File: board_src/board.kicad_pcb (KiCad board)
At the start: 2 copper layers, 220 x 150 mm, 149 parts, among them IC1 PCF8563TS_4,118, IC2 M24C02-WMN6TP, IC3 DS18B20+, IC4 FT232RNL-TUBE, IC5 MCP3202, IC6 MCP4921-E_P, J1 Conn_01x05, J10 Conn_01x02_Pin, J11 Conn_01x03, J12 112J-TDAR-R01, J13 Conn_01x03, J14 Conn_01x07, J15 Conn_01x03, J16 Conn_01x05, J17 Conn_01x05, J18 Conn_02x20_Counter_Clockwise, J19 Conn_02x07_Odd_Even, J2 Conn_01x05, J20 Conn_02x20_Counter_Clockwise, J21 Conn_02x20_Counter_Clockwise, J22 Conn_02x20_Counter_Clockwise, J23 Conn_01x04, J24 Conn_01x08, J25 Conn_01x04, J26 Conn_01x20_Socket, J27 Conn_01x20_Socket, J28 Conn_01x04, J29 Conn_01x08, J3 Conn_01x06, J30 Conn_01x05, J31 Conn_01x05, J32 Conn_02x05_Odd_Even, J33 Conn_01x02_Pin, J34 USB_C_Receptacle_USB2.0_16P, J36 Conn_01x20_Socket, J37 Conn_01x20_Socket, J4 Conn_01x04, J40 Conn_01x01_Pin, J41 Conn_01x01_Pin, J42 Conn_01x01_Pin, J43 Conn_01x01_Pin, J44 Conn_01x01_Pin, J46 Conn_01x01_Pin, J5 Conn_01x08, J6 Conn_01x02_Pin, J7 Conn_01x16_Socket, J8 Conn_01x04, J9 Conn_01x02_Pin, Q1 NPN, Q2 SS8550, Q3 SS8550, Q4 SS8550, Q5 SS8550, Q6 BSS123, Q7 BC107, Y2 Crystal

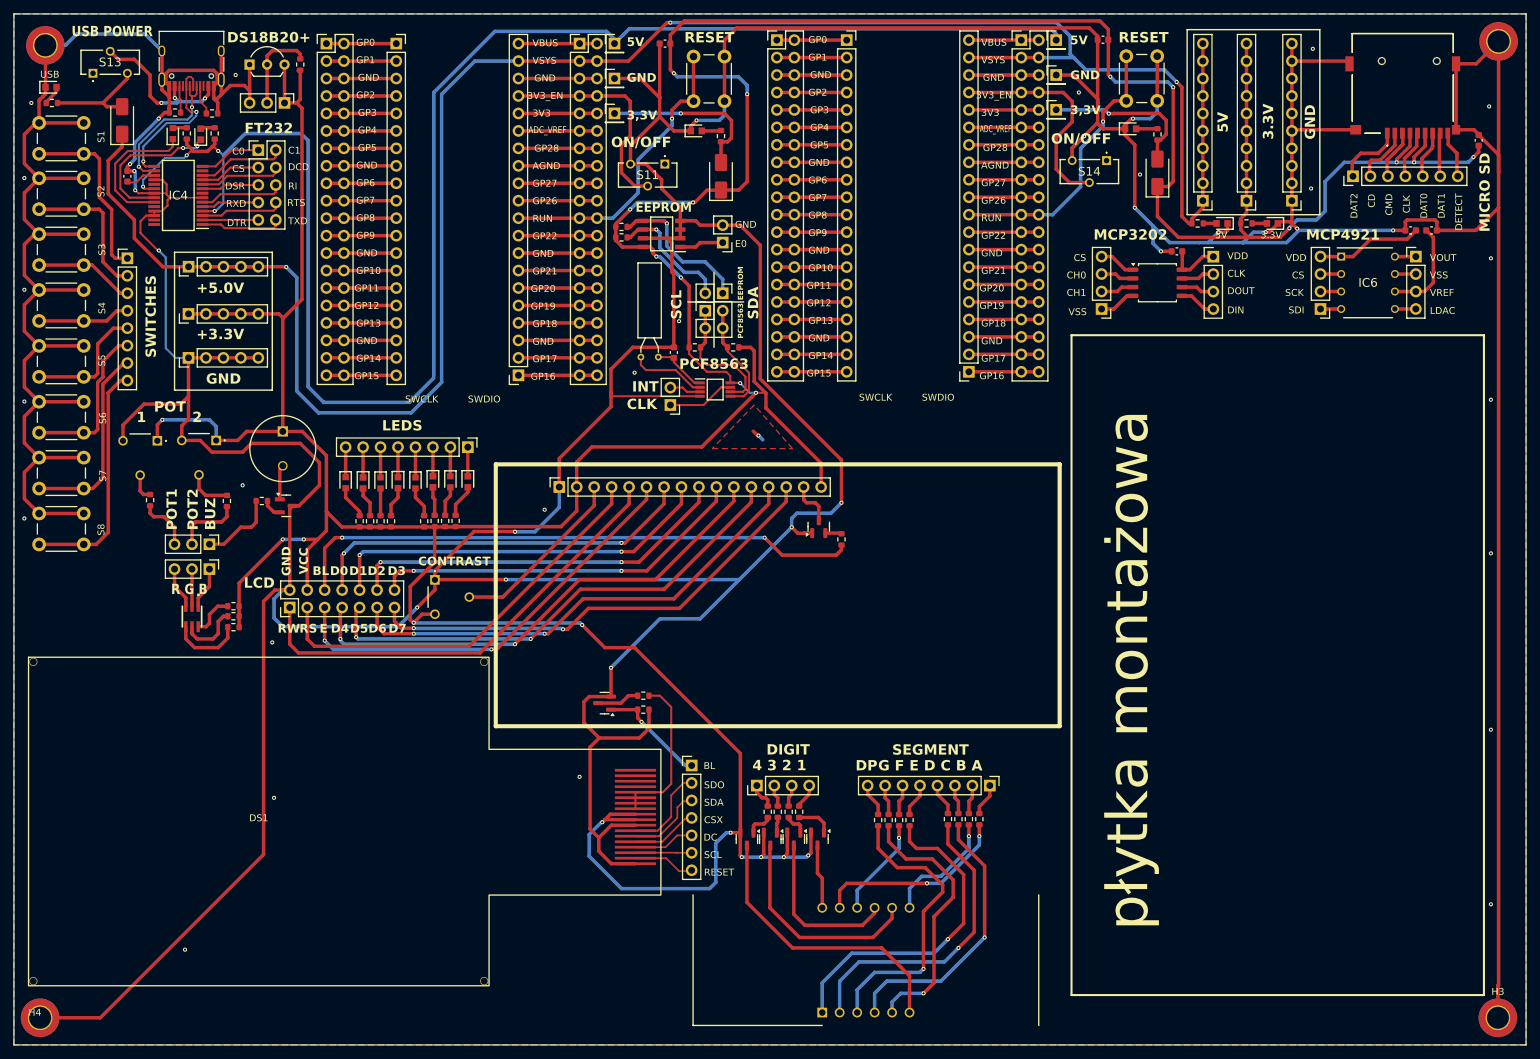
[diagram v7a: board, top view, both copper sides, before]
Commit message: Poprawki w schematach. Rozpoczęte korekty płytki
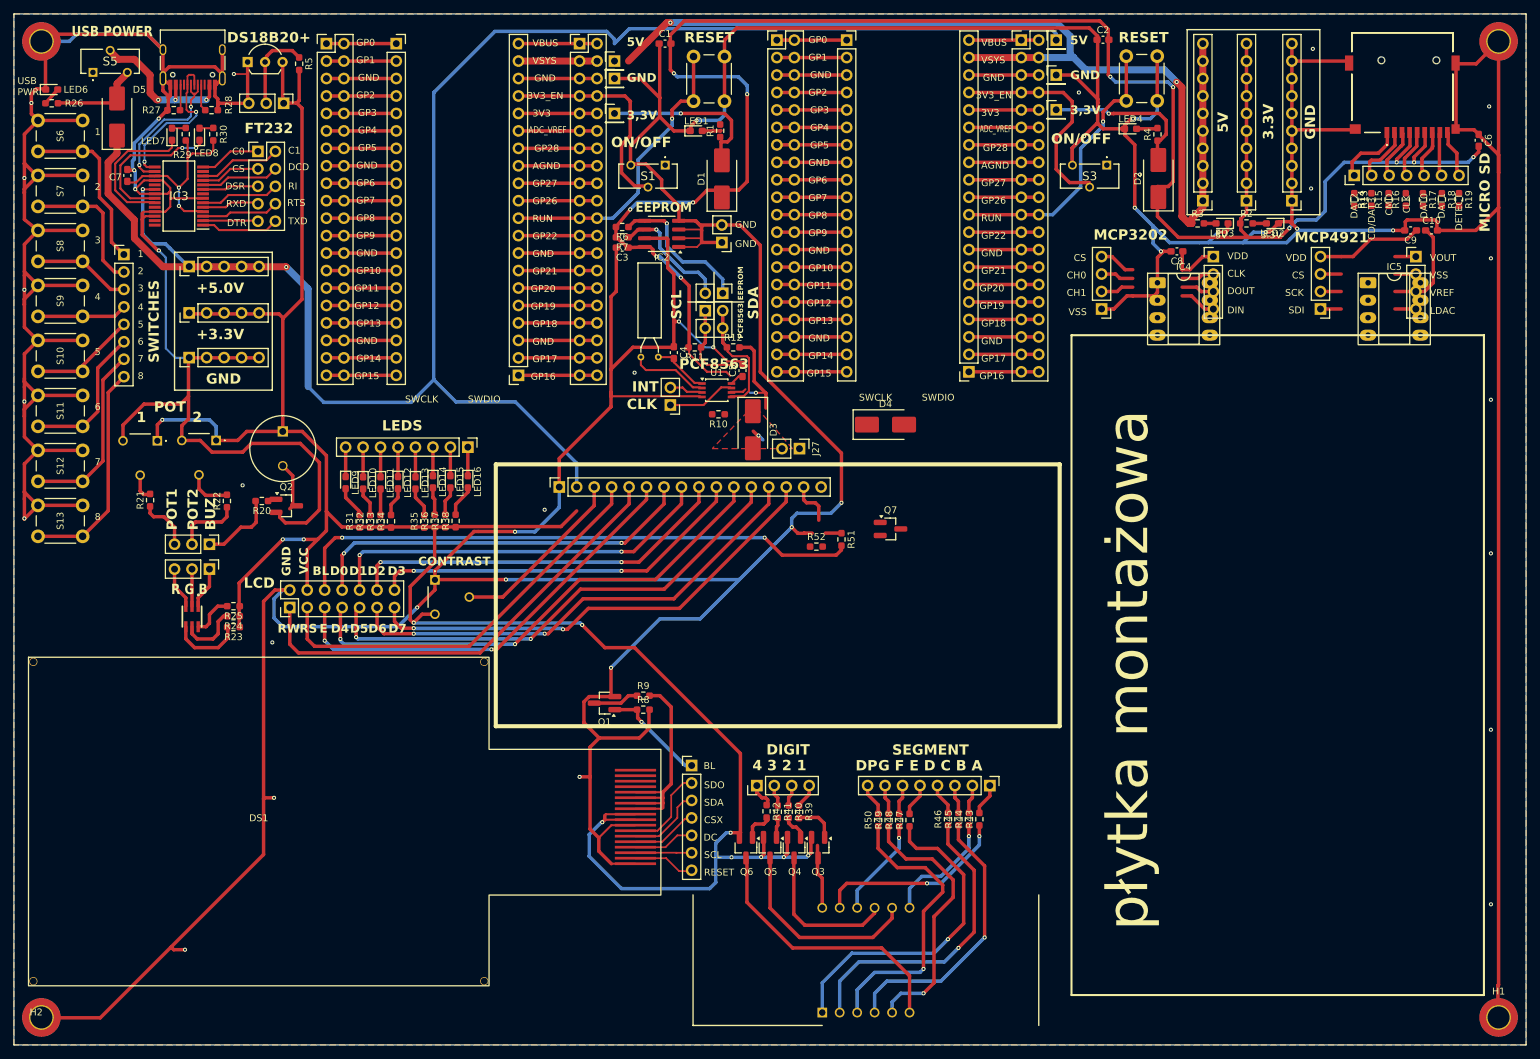
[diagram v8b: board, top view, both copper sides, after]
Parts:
- removed the IC1 at (102.0, 54.7)
- added C3: 100n, Capacitor_SMD:C_0603_1608Metric_Pad1.08x0.95mm_HandSolder, F.Cu at (88.5, 34.0)
- added C5: 100n, Capacitor_SMD:C_0603_1608Metric_Pad1.08x0.95mm_HandSolder, F.Cu at (106.0, 51.9)
- added D1: VS-10BQ015-M3/5BT, Diode_SMD:D_SMB_Handsoldering, F.Cu at (103.0, 24.0)
- added D3: VS-10BQ015-M3/5BT, Diode_SMD:D_SMB_Handsoldering, F.Cu at (107.5, 60.5)
- added J27: Battery, Connector_PinHeader_2.54mm:PinHeader_1x02_P2.54mm_Vertical, F.Cu at (114.3, 63.2)
- added R10: 47k, Resistor_SMD:R_0603_1608Metric_Pad0.98x0.95mm_HandSolder, F.Cu at (102.5, 58.2)
- added R13: 47k, Resistor_SMD:R_0603_1608Metric_Pad0.98x0.95mm_HandSolder, F.Cu at (195.0, 27.0)
- added R14: 47k, Resistor_SMD:R_0603_1608Metric_Pad0.98x0.95mm_HandSolder, F.Cu at (197.5, 27.0)
- added R15: 47k, Resistor_SMD:R_0603_1608Metric_Pad0.98x0.95mm_HandSolder, F.Cu at (200.0, 27.0)
- added R16: 47k, Resistor_SMD:R_0603_1608Metric_Pad0.98x0.95mm_HandSolder, F.Cu at (202.5, 27.0)
- added R17: 47k, Resistor_SMD:R_0603_1608Metric_Pad0.98x0.95mm_HandSolder, F.Cu at (205.0, 27.0)
- added R18: 47k, Resistor_SMD:R_0603_1608Metric_Pad0.98x0.95mm_HandSolder, F.Cu at (207.8, 27.0)
- added R19: 47k, Resistor_SMD:R_0603_1608Metric_Pad0.98x0.95mm_HandSolder, F.Cu at (210.2, 27.0)
- added R52: 50, Resistor_SMD:R_0603_1608Metric_Pad0.98x0.95mm_HandSolder, F.Cu at (116.8, 77.5)
- added U1: PCF8563TS, Package_SO:TSSOP-8_3x3mm_P0.65mm, F.Cu at (102.2, 54.8)
- C1: renamed from C5; footprint Capacitor_SMD:C_0603_1608Metric -> Capacitor_SMD:C_0603_1608Metric_Pad1.08x0.95mm_HandSolder
- C10: renamed from C8; footprint Capacitor_SMD:C_0603_1608Metric -> Capacitor_SMD:C_0603_1608Metric_Pad1.08x0.95mm_HandSolder
- C2: renamed from C6; footprint Capacitor_SMD:C_0603_1608Metric -> Capacitor_SMD:C_0603_1608Metric_Pad1.08x0.95mm_HandSolder
- C4: renamed from C1; value 100n -> 10p; footprint Capacitor_SMD:C_0603_1608Metric -> Capacitor_SMD:C_0603_1608Metric_Pad1.08x0.95mm_HandSolder
- C6: renamed from C3; footprint Capacitor_SMD:C_0603_1608Metric -> Capacitor_SMD:C_0603_1608Metric_Pad1.08x0.95mm_HandSolder
- C7: renamed from C2; value C_Small -> 100n; footprint Capacitor_SMD:C_0603_1608Metric -> Capacitor_SMD:C_0603_1608Metric_Pad1.08x0.95mm_HandSolder
- C8: renamed from C4; footprint Capacitor_SMD:C_0603_1608Metric -> Capacitor_SMD:C_0603_1608Metric_Pad1.08x0.95mm_HandSolder
- C9: renamed from C7; footprint Capacitor_SMD:C_0603_1608Metric -> Capacitor_SMD:C_0603_1608Metric_Pad1.08x0.95mm_HandSolder
- D2, D4, D5: value D_Schottky -> VS-10BQ015-M3/5BT; footprint Diode_SMD:D_SMA -> Diode_SMD:D_SMB_Handsoldering
- IC2: footprint footprints:EEPROM -> Package_SO:SOIC-8_3.9x4.9mm_P1.27mm
- IC4: renamed from IC5; footprint Package_SO:SOIC-8_5.3x5.3mm_P1.27mm -> Package_DIP:DIP-8_W7.62mm_Socket_LongPads
- IC5: renamed from IC6; footprint footprints:DIP781W56P254L950H533Q8N -> Package_DIP:DIP-8_W7.62mm_Socket_LongPads
- LED1: renamed from LED14; footprint footprints:LEDC1608X100N -> LED_SMD:LED_0603_1608Metric_Pad1.05x0.95mm_HandSolder
- LED10: renamed from LED6; footprint footprints:LEDC1608X100N -> LED_SMD:LED_0603_1608Metric_Pad1.05x0.95mm_HandSolder
- LED11: renamed from LED3; footprint footprints:LEDC1608X80N -> LED_SMD:LED_0603_1608Metric_Pad1.05x0.95mm_HandSolder
- LED12: renamed from LED7; footprint footprints:LEDC1608X100N -> LED_SMD:LED_0603_1608Metric_Pad1.05x0.95mm_HandSolder
- LED13: renamed from LED4; footprint footprints:LEDC1608X80N -> LED_SMD:LED_0603_1608Metric_Pad1.05x0.95mm_HandSolder
- LED14: renamed from LED8; footprint footprints:LEDC1608X100N -> LED_SMD:LED_0603_1608Metric_Pad1.05x0.95mm_HandSolder
- LED15: renamed from LED5; footprint footprints:LEDC1608X80N -> LED_SMD:LED_0603_1608Metric_Pad1.05x0.95mm_HandSolder
- LED16: renamed from LED9; footprint footprints:LEDC1608X100N -> LED_SMD:LED_0603_1608Metric_Pad1.05x0.95mm_HandSolder
- LED2: renamed from LED16; footprint footprints:LEDC1608X100N -> LED_SMD:LED_0603_1608Metric_Pad1.05x0.95mm_HandSolder
- LED3: renamed from LED17; footprint footprints:LEDC1608X100N -> LED_SMD:LED_0603_1608Metric_Pad1.05x0.95mm_HandSolder
- LED4: renamed from LED15; footprint footprints:LEDC1608X100N -> LED_SMD:LED_0603_1608Metric_Pad1.05x0.95mm_HandSolder
- LED6: renamed from LED18; footprint footprints:LEDC1608X100N -> LED_SMD:LED_0603_1608Metric_Pad1.05x0.95mm_HandSolder
- LED7: renamed from LED10; footprint footprints:LEDC1608X80N -> LED_SMD:LED_0603_1608Metric_Pad1.05x0.95mm_HandSolder
- LED8: renamed from LED11; footprint footprints:LEDC1608X100N -> LED_SMD:LED_0603_1608Metric_Pad1.05x0.95mm_HandSolder
- LED9: renamed from LED2; footprint footprints:LEDC1608X80N -> LED_SMD:LED_0603_1608Metric_Pad1.05x0.95mm_HandSolder
- LS1: value BMT0905XH05 -> UGCM0903XP4.5IC
- Q1: renamed from Q6; footprint Package_TO_SOT_SMD:SOT-23 -> Package_TO_SOT_SMD:SOT-23_Handsoldering
- Q2: renamed from Q1; value NPN -> SS8050-L; footprint Package_TO_SOT_SMD:SOT-23 -> Package_TO_SOT_SMD:SOT-23_Handsoldering
- Q3: renamed from Q2; value SS8550 -> SS8550-L; footprint Package_TO_SOT_SMD:SOT-23 -> Package_TO_SOT_SMD:SOT-23_Handsoldering
- Q4: renamed from Q3; value SS8550 -> SS8550-L; footprint Package_TO_SOT_SMD:SOT-23 -> Package_TO_SOT_SMD:SOT-23_Handsoldering
- Q5: renamed from Q4; value SS8550 -> SS8550-L; footprint Package_TO_SOT_SMD:SOT-23 -> Package_TO_SOT_SMD:SOT-23_Handsoldering
- Q6: renamed from Q5; value SS8550 -> SS8550-L; footprint Package_TO_SOT_SMD:SOT-23 -> Package_TO_SOT_SMD:SOT-23_Handsoldering
- Q7: value BC107 -> SS8050-L; footprint Package_TO_SOT_SMD:SOT-23 -> Package_TO_SOT_SMD:SOT-23_Handsoldering
- R1: renamed from R6; footprint Resistor_SMD:R_0603_1608Metric -> Resistor_SMD:R_0603_1608Metric_Pad0.98x0.95mm_HandSolder
- R11: renamed from R43; value 4.7k -> 10k; footprint Resistor_SMD:R_0603_1608Metric -> Resistor_SMD:R_0603_1608Metric_Pad0.98x0.95mm_HandSolder
- R12: renamed from R44; value 4.7k -> 10k; footprint Resistor_SMD:R_0603_1608Metric -> Resistor_SMD:R_0603_1608Metric_Pad0.98x0.95mm_HandSolder
- R2: renamed from R8; footprint Resistor_SMD:R_0603_1608Metric -> Resistor_SMD:R_0603_1608Metric_Pad0.98x0.95mm_HandSolder
- R20: value 450 -> 4.7k; footprint Resistor_SMD:R_0603_1608Metric -> Resistor_SMD:R_0603_1608Metric_Pad0.98x0.95mm_HandSolder
- R21: renamed from R2; value 270 -> 27; footprint Resistor_SMD:R_0603_1608Metric -> Resistor_SMD:R_0603_1608Metric_Pad0.98x0.95mm_HandSolder
- R22: renamed from R14; value 270 -> 27; footprint Resistor_SMD:R_0603_1608Metric -> Resistor_SMD:R_0603_1608Metric_Pad0.98x0.95mm_HandSolder
- R23: footprint Resistor_SMD:R_0603_1608Metric -> Resistor_SMD:R_0603_1608Metric_Pad0.98x0.95mm_HandSolder
- R24: renamed from R22; footprint Resistor_SMD:R_0603_1608Metric -> Resistor_SMD:R_0603_1608Metric_Pad0.98x0.95mm_HandSolder
- R25: renamed from R21; footprint Resistor_SMD:R_0603_1608Metric -> Resistor_SMD:R_0603_1608Metric_Pad0.98x0.95mm_HandSolder
- R26: renamed from R10; value 249 -> 330; footprint Resistor_SMD:R_0603_1608Metric -> Resistor_SMD:R_0603_1608Metric_Pad0.98x0.95mm_HandSolder
- R27: renamed from R46; footprint Resistor_SMD:R_0603_1608Metric -> Resistor_SMD:R_0603_1608Metric_Pad0.98x0.95mm_HandSolder
- R28: renamed from R45; footprint Resistor_SMD:R_0603_1608Metric -> Resistor_SMD:R_0603_1608Metric_Pad0.98x0.95mm_HandSolder
- R29: renamed from R5; value 1k -> 220; footprint Resistor_SMD:R_0603_1608Metric -> Resistor_SMD:R_0603_1608Metric_Pad0.98x0.95mm_HandSolder
- R3: renamed from R9; footprint Resistor_SMD:R_0603_1608Metric -> Resistor_SMD:R_0603_1608Metric_Pad0.98x0.95mm_HandSolder
- R30: renamed from R3; value 1k -> 220; footprint Resistor_SMD:R_0603_1608Metric -> Resistor_SMD:R_0603_1608Metric_Pad0.98x0.95mm_HandSolder
- R31: renamed from R11; footprint Resistor_SMD:R_0603_1608Metric -> Resistor_SMD:R_0603_1608Metric_Pad0.98x0.95mm_HandSolder
- R32: renamed from R12; footprint Resistor_SMD:R_0603_1608Metric -> Resistor_SMD:R_0603_1608Metric_Pad0.98x0.95mm_HandSolder
- R33: renamed from R37; footprint Resistor_SMD:R_0603_1608Metric -> Resistor_SMD:R_0603_1608Metric_Pad0.98x0.95mm_HandSolder
- R34: renamed from R38; footprint Resistor_SMD:R_0603_1608Metric -> Resistor_SMD:R_0603_1608Metric_Pad0.98x0.95mm_HandSolder
- R35: renamed from R39; footprint Resistor_SMD:R_0603_1608Metric -> Resistor_SMD:R_0603_1608Metric_Pad0.98x0.95mm_HandSolder
- R36: renamed from R40; footprint Resistor_SMD:R_0603_1608Metric -> Resistor_SMD:R_0603_1608Metric_Pad0.98x0.95mm_HandSolder
- R37: renamed from R41; footprint Resistor_SMD:R_0603_1608Metric -> Resistor_SMD:R_0603_1608Metric_Pad0.98x0.95mm_HandSolder
- R38: renamed from R42; footprint Resistor_SMD:R_0603_1608Metric -> Resistor_SMD:R_0603_1608Metric_Pad0.98x0.95mm_HandSolder
- R39: renamed from R31; footprint Resistor_SMD:R_0603_1608Metric -> Resistor_SMD:R_0603_1608Metric_Pad0.98x0.95mm_HandSolder
- R4: renamed from R7; footprint Resistor_SMD:R_0603_1608Metric -> Resistor_SMD:R_0603_1608Metric_Pad0.98x0.95mm_HandSolder
- R40: renamed from R32; footprint Resistor_SMD:R_0603_1608Metric -> Resistor_SMD:R_0603_1608Metric_Pad0.98x0.95mm_HandSolder
- R41: renamed from R33; footprint Resistor_SMD:R_0603_1608Metric -> Resistor_SMD:R_0603_1608Metric_Pad0.98x0.95mm_HandSolder
- R42: renamed from R34; footprint Resistor_SMD:R_0603_1608Metric -> Resistor_SMD:R_0603_1608Metric_Pad0.98x0.95mm_HandSolder
- R43: renamed from R13; value 220 -> 330; footprint Resistor_SMD:R_0603_1608Metric -> Resistor_SMD:R_0603_1608Metric_Pad0.98x0.95mm_HandSolder
- R44: renamed from R24; footprint Resistor_SMD:R_0603_1608Metric -> Resistor_SMD:R_0603_1608Metric_Pad0.98x0.95mm_HandSolder
- R45: renamed from R25; value 220 -> 330; footprint Resistor_SMD:R_0603_1608Metric -> Resistor_SMD:R_0603_1608Metric_Pad0.98x0.95mm_HandSolder
- R46: renamed from R26; value 220 -> 330; footprint Resistor_SMD:R_0603_1608Metric -> Resistor_SMD:R_0603_1608Metric_Pad0.98x0.95mm_HandSolder
- R47: renamed from R27; value 220 -> 330; footprint Resistor_SMD:R_0603_1608Metric -> Resistor_SMD:R_0603_1608Metric_Pad0.98x0.95mm_HandSolder
- R48: renamed from R28; value 220 -> 330; footprint Resistor_SMD:R_0603_1608Metric -> Resistor_SMD:R_0603_1608Metric_Pad0.98x0.95mm_HandSolder
- R49: renamed from R29; value 220 -> 330; footprint Resistor_SMD:R_0603_1608Metric -> Resistor_SMD:R_0603_1608Metric_Pad0.98x0.95mm_HandSolder
- R5: renamed from R19; value 4.7k -> 10k; footprint Resistor_SMD:R_0603_1608Metric -> Resistor_SMD:R_0603_1608Metric_Pad0.98x0.95mm_HandSolder
- R50: renamed from R30; value 220 -> 330; footprint Resistor_SMD:R_0603_1608Metric -> Resistor_SMD:R_0603_1608Metric_Pad0.98x0.95mm_HandSolder
- R51: renamed from R4; footprint Resistor_SMD:R_0603_1608Metric -> Resistor_SMD:R_0603_1608Metric_Pad0.98x0.95mm_HandSolder
- R6: renamed from R15; value 4.7k -> 10k; footprint Resistor_SMD:R_0603_1608Metric -> Resistor_SMD:R_0603_1608Metric_Pad0.98x0.95mm_HandSolder
- R7: renamed from R16; value 4.7k -> 10k; footprint Resistor_SMD:R_0603_1608Metric -> Resistor_SMD:R_0603_1608Metric_Pad0.98x0.95mm_HandSolder
- R8: renamed from R1; footprint Resistor_SMD:R_0603_1608Metric -> Resistor_SMD:R_0603_1608Metric_Pad0.98x0.95mm_HandSolder
- R9: renamed from R17; footprint Resistor_SMD:R_0603_1608Metric -> Resistor_SMD:R_0603_1608Metric_Pad0.98x0.95mm_HandSolder
- RV1: value R_Potentiometer -> 10K
- VR1, VR2: value PT6KV-251A2020 -> PT6KV-103A20-PM
- Y1: renamed from Y2; value Crystal -> 32.768kHz
- moved D5 151.6 mm to (15.0, 15.0)
- moved D2 151.0 mm to (166.5, 23.9)
- moved D4 43.3 mm to (126.8, 59.8), turned to 0 degrees
- moved Q7 10.4 mm to (127.5, 74.9), turned to 0 degrees
- moved J8 2.54 mm to (87.4, 6.86)
- moved R6 1.52 mm to (88.5, 31.0)
- moved R7 1.52 mm to (88.5, 32.5)
- moved Q3 1.27 mm to (117.0, 121.3)
- moved Q4 1.26 mm to (113.5, 121.3)
- moved Q6 1.24 mm to (106.5, 121.3)
- moved Q5 1.24 mm to (110.0, 121.3)
- moved S13 1.19 mm to (10.0, 76.0)
- moved S12 1.06 mm to (10.0, 68.0)
- moved S11 0.94 mm to (10.0, 60.0)
- moved S10 0.81 mm to (10.0, 52.0)
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- renumbered H3 to H1, H4 to H2, H2 to H3, H1 to H4, IC3 to IC1, IC4 to IC3, J18 to J1, J30 to J10, J31 to J11, J2 to J12, J20 to J13, J21 to J14, J27 to J15, J36 to J16, J41 to J17, J44 to J18, J46 to J19, J26 to J2, J22 to J20, J11 to J21, J33 to J22, J6 to J23, J3 to J24, J9 to J25, J10 to J26, J14 to J28, J12 to J29, J37 to J3, J13 to J30, J15 to J31, J34 to J33, J29 to J34, J23 to J35, J4 to J36, J5 to J37, J25 to J38, J24 to J39, J16 to J4, J7 to J40, J19 to J41, J28 to J42, J8 to J43, J17 to J5, J1 to J6, J40 to J7, J42 to J8, J43 to J9, LED1 to LED5, S11 to S1, S5 to S10, S6 to S11, S7 to S12, S8 to S13, S1 to S2, S14 to S3, S12 to S4, S13 to S5, S1 to S6, S2 to S7, S3 to S8, S4 to S9
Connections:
- net /Port USB/C3 renamed /Port USB/CB3
- net /Port USB/C4 renamed /Port USB/CB4
- net /Wyświetlacz/KATODA renamed Net-(DS1-LED-K-Pad11)
- net /Wyświetlacz/R0 renamed /Wyświetlacz/EL
- C7 pad 1: Net-(IC4-3V3OUT) -> /Port USB/3V3OUT
- D2 pad 1: VSYS -> +3.3V
- D4 pad 1: +3.3V -> Net-(D3-K)
- D4 pad 2: Net-(D4-A) -> +3.3V
- D5 pad 1: +3.3V -> +5V
- IC2 pad 1: Net-(IC2-E0) -> GND
- IC3 pad 17: Net-(IC4-3V3OUT) -> /Port USB/3V3OUT
- IC3 pad 4: +5V -> /Port USB/3V3OUT
- IC4 pad 4: Net-(IC5-VSS) -> GND
- IC5 pad 7: Net-(IC6-VSS) -> GND
- J11 pad 1: VSYS -> +5V
- J11 pad 10: VSYS -> +5V
- J11 pad 2: VSYS -> +5V
- J11 pad 3: VSYS -> +5V
- J11 pad 4: VSYS -> +5V
- J11 pad 5: VSYS -> +5V
- J11 pad 6: VSYS -> +5V
- J11 pad 7: VSYS -> +5V
- J11 pad 8: VSYS -> +5V
- J11 pad 9: VSYS -> +5V
- J13 pad 3: VSYS -> +5.0V
- J13 pad 4: VSYS -> +5V
- J16 pad 19: VSYS -> +5V
- J17 pad 1: Net-(D5-A) -> Net-(D2-A)
- J20 pad 3: VSYS -> +5V
- J20 pad 4: VSYS -> +5V
- J22 pad 1: Net-(IC2-E0) -> GND
- J23 pad 1: Net-(IC2-SDA) -> Net-(IC2-SCL)
- J23 pad 2: Net-(IC2-SCL) -> Net-(IC2-SDA)
- J29 pad 6: +3.3V -> GND
- J3 pad 19: VSYS -> +5V
- J31 pad 1: Net-(J15-Pin_3) -> Net-(J31-Pin_1)
- J31 pad 3: Net-(J15-Pin_1) -> Net-(J31-Pin_3)
- J35 pad 1: Net-(IC5-VSS) -> GND
- J40 pad 15: Net-(J7-Pin_15) -> Net-(J40-Pin_15)
- J40 pad 16: +3.3V -> Net-(J40-Pin_16)
- J40 pad 2: +3.3V -> +5V
- J40 pad 5: /Wyświetlacz LCD/R/W -> GND
- J41 pad 1: /Wyświetlacz LCD/R/W -> GND
- J43 pad 2: Net-(IC6-VSS) -> GND
- J5 pad 1: VSYS -> +5V
- J5 pad 2: VSYS -> +5V
- J5 pad 3: VSYS -> +5V
- J5 pad 4: VSYS -> +5V
- J5 pad 5: VSYS -> +5V
- J7 pad 1: Net-(D4-A) -> Net-(D1-A)
- LED5 pad 1: Net-(J15-Pin_3) -> Net-(J31-Pin_3)
- LED5 pad 3: Net-(J15-Pin_1) -> Net-(J31-Pin_1)
- LS1 pad 1: +3.3V -> +5V
- Q2 pad 1: Net-(LS1--) -> Net-(Q2-B)
- Q2 pad 2: Net-(Q1-B) -> GND
- Q2 pad 3: GND -> Net-(LS1--)
- Q7 pad 1: GND -> Net-(Q7-B)
- Q7 pad 2: Net-(Q7-B) -> GND
- Q7 pad 3: Net-(J7-Pin_15) -> Net-(J40-Pin_16)
- R1 pad 1: Net-(D4-A) -> Net-(D1-A)
- R20 pad 1: Net-(Q1-B) -> Net-(Q2-B)
- R26 pad 1: Net-(D2-A) -> Net-(D5-A)
- R29 pad 1: +5V -> /Port USB/3V3OUT
- R3 pad 1: VSYS -> +5V
- R30 pad 1: +5V -> /Port USB/3V3OUT
- R4 pad 1: Net-(D5-A) -> Net-(D2-A)
- R51 pad 1: Net-(Q7-B) -> /Wyświetlacz LCD/BL
- R51 pad 2: /Wyświetlacz LCD/BL -> Net-(Q7-B)
- R6 pad 1: Net-(IC2-SCL) -> Net-(IC2-SDA)
- R7 pad 1: Net-(IC2-SDA) -> Net-(IC2-SCL)
- RV1 pad 1: +3.3V -> +5V
- S5 pad 3: Net-(D2-A) -> Net-(D5-A)
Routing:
- net VSYS: track 306.4 -> 0.00 mm, vias 3 -> 0
- net +5V: track 240.6 -> 416.6 mm
- net GND: track 1227.3 -> 1399.2 mm, vias 21 -> 30
- net /Wyświetlacz LCD/R/W: track 66.7 -> 0.00 mm
- net +3.3V: track 699.5 -> 643.4 mm, vias 25 -> 24
- net /Port USB/3V3OUT: track 0.00 -> 28.4 mm, vias 0 -> 2
- net (no net): track 0.00 -> 26.4 mm, vias 24 -> 14
- net Net-(D4-A): track 24.8 -> 0.00 mm, vias 1 -> 0
- net Net-(D1-A): track 0.00 -> 24.8 mm, vias 0 -> 1
- net Net-(IC5-VREF): track 14.2 -> 0.00 mm
- net Net-(DS1-LED-K-Pad11): track 23.2 -> 35.1 mm
- net +5.0V: track 0.00 -> 11.4 mm
- net Net-(D5-A): track 23.1 -> 13.9 mm, vias 1 -> 0
- net Net-(D2-A): track 15.4 -> 23.1 mm, vias 0 -> 1
- net Net-(J7-Pin_15): track 6.48 -> 0.00 mm
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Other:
- board text added: "3"
- board text added: "4"
- board text added: "5"
- board text added: "6"
- board text added: "7"
- board text added: "8"
- board text added: "CD/DAT3"
- board text added: "USB PWR"
- board text removed: "CD"
- board text removed: "E0"
- board text removed: "USB"
